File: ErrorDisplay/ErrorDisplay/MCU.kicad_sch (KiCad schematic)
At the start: 0 parts

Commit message: WIP checkin
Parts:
- added BZ1: Buzzer, symbol Device:Buzzer
- added C6, C7: 0.1u, Capacitor_SMD:C_0402_1005Metric_Pad0.74x0.62mm_HandSolder, symbol Device:C
- added D1: LED, LED_SMD:LED_0603_1608Metric_Pad1.05x0.95mm_HandSolder, symbol Device:LED
- added J6: Conn_01x02_Pin, Connector_PinHeader_1.27mm:PinHeader_1x02_P1.27mm_Vertical, symbol Connector:Conn_01x02_Pin
- added J7: Conn_01x02_Pin, Connector_PinHeader_1.00mm:PinHeader_1x02_P1.00mm_Vertical, symbol Connector:Conn_01x02_Pin
- added Q1: NMOS, symbol Simulation_SPICE:NMOS
- added R17: 4.7k, Resistor_SMD:R_0402_1005Metric_Pad0.72x0.64mm_HandSolder, symbol Device:R
- added R23: 100k, Resistor_SMD:R_0402_1005Metric_Pad0.72x0.64mm_HandSolder, symbol Device:R
- added R24: TBD, Resistor_SMD:R_0402_1005Metric, symbol Device:R
- added U5: ~, X27:SFH_5711-23-Z, symbol New_Library:SFH_5711-2/3-Z
- added U6: STM32G0B1KBTx, Package_QFP:LQFP-32_7x7mm_P0.8mm, symbol MCU_ST_STM32G0:STM32G0B1KBTx
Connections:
- new net: BZ1.2 (-), Q1.1 (D)
- new net: D1.1 (K), R17.1
- new net +3V3: C6.1, C7.1, J6.2 (Pin_2), U5.3 (VCC), U6.4 (VDD)
- new net +5V: BZ1.1 (+)
- new net AMB_OUT: J6.1 (Pin_1), J7.2 (Pin_2), R24.1, U5.4 (OUT)
- new net Buzzer: Q1.2 (G), R23.1
- new net GND: C6.2, C7.2, J7.1 (Pin_1), Q1.3 (S), R17.2, R23.2, R24.2, U5.1 (GND), U5.2 (GND), U6.5 (VSS)
- new net HB: D1.2 (A)
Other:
- note added: "1uA->50uA based on no light to all light"
- note added: "Connector for decade box for testing"
- note added: "Photodetector path i.e. CdS photoresistor"
- note added: "TODO"
- note added: "TODO need to confirm this"

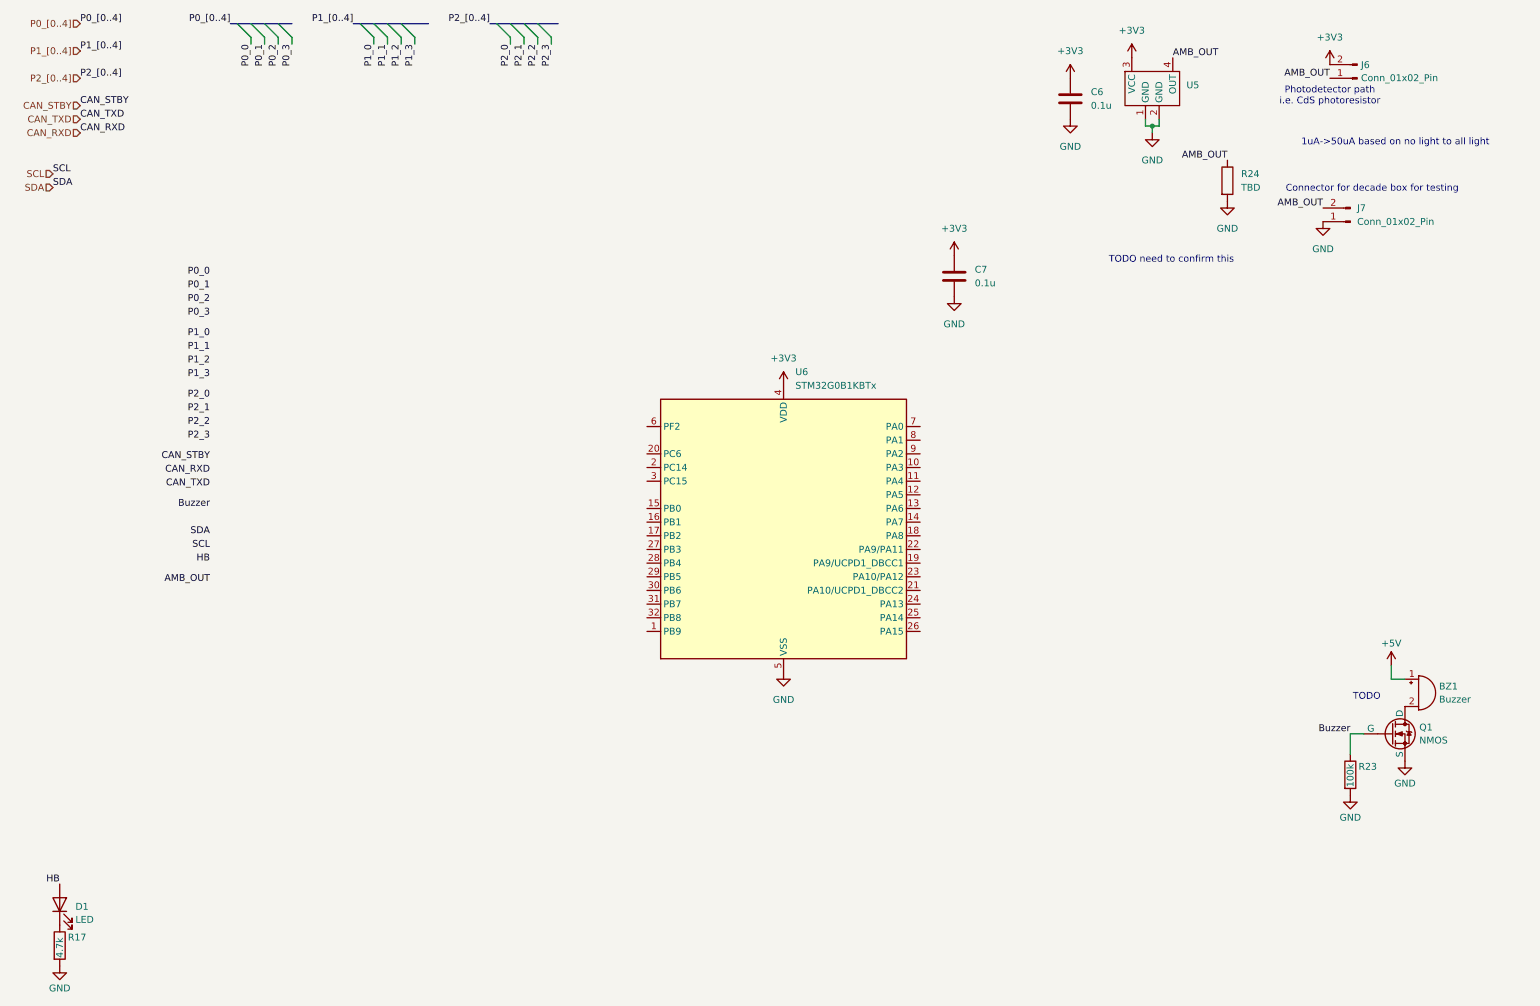
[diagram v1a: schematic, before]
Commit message: Added Buzzer, Fet Footprint, and pulled backlighting
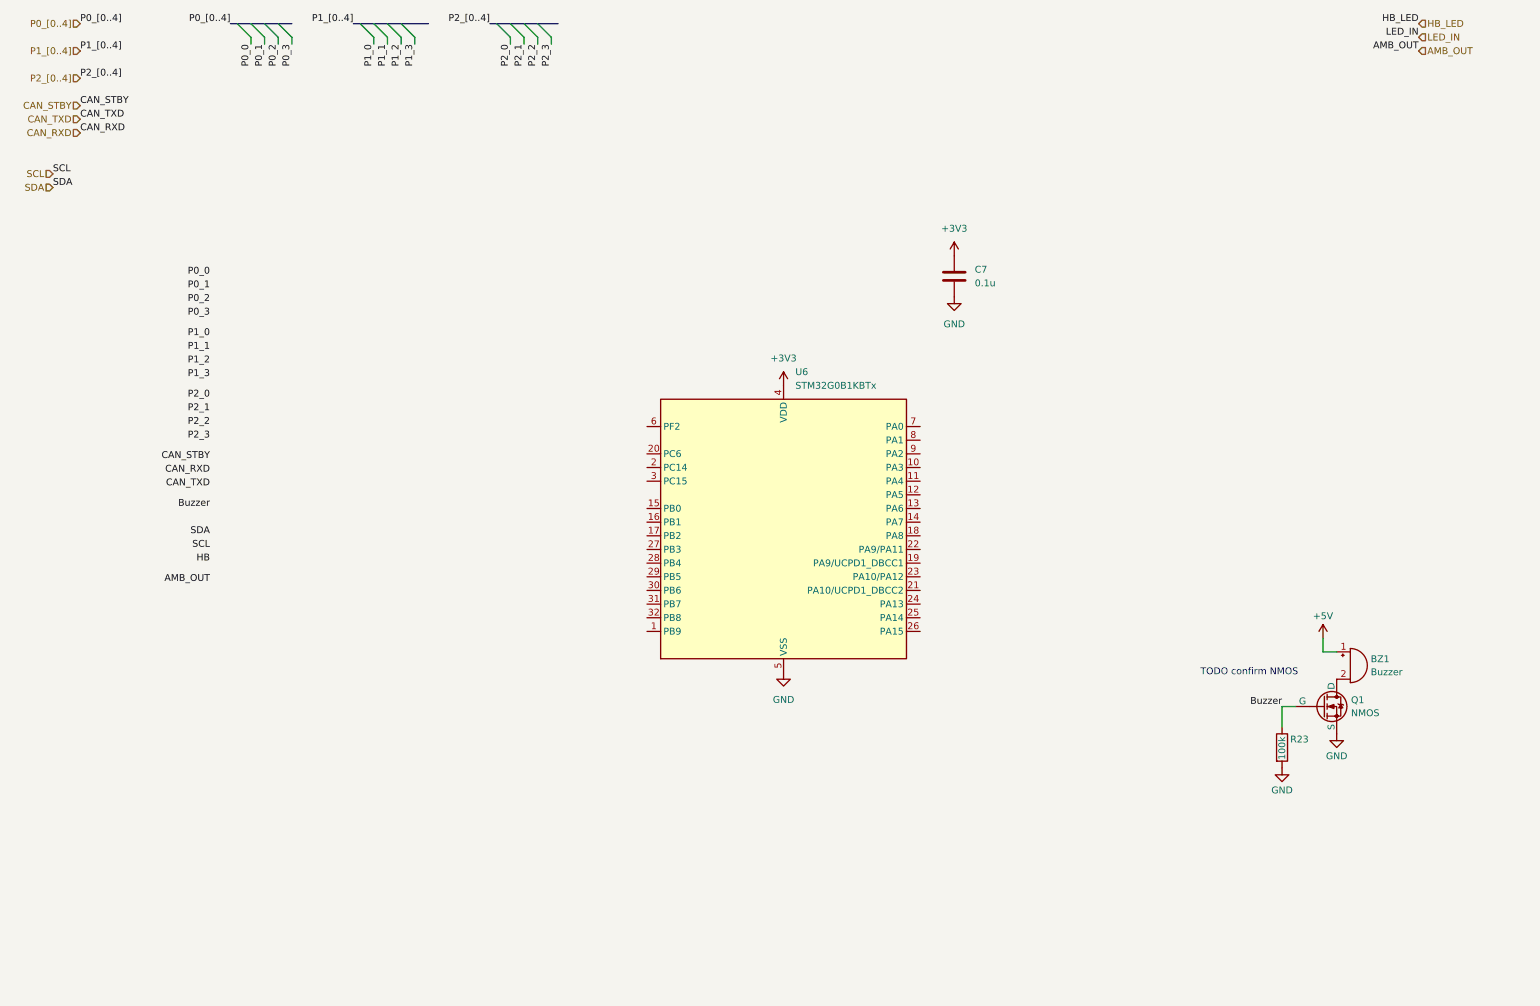
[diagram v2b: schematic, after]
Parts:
- removed C6: 0.1u, Capacitor_SMD:C_0402_1005Metric_Pad0.74x0.62mm_HandSolder, symbol Device:C
- removed D1: LED, LED_SMD:LED_0603_1608Metric_Pad1.05x0.95mm_HandSolder, symbol Device:LED
- removed J6: Conn_01x02_Pin, Connector_PinHeader_1.27mm:PinHeader_1x02_P1.27mm_Vertical, symbol Connector:Conn_01x02_Pin
- removed J7: Conn_01x02_Pin, Connector_PinHeader_1.00mm:PinHeader_1x02_P1.00mm_Vertical, symbol Connector:Conn_01x02_Pin
- removed R17: 4.7k, Resistor_SMD:R_0402_1005Metric_Pad0.72x0.64mm_HandSolder, symbol Device:R
- removed R24: TBD, Resistor_SMD:R_0402_1005Metric, symbol Device:R
- removed U5: ~, X27:SFH_5711-23-Z, symbol New_Library:SFH_5711-2/3-Z
- BZ1: footprint (none) -> Library:CEM-1205-IC
- Q1: footprint (none) -> Library:SC-59_Handsoldering
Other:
- note added: "TODO confirm NMOS"
- note removed: "1uA->50uA based on no light to all light"
- note removed: "Connector for decade box for testing"
- note removed: "Photodetector path i.e. CdS photoresistor"
- note removed: "TODO"
- note removed: "TODO need to confirm this"
- moved on the sheet: BZ1, Q1, R23
